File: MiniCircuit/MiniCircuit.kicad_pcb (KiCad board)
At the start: 2 copper layers, 114 x 96.5 mm, 49 parts, among them J1 Conn_02x16_Odd_Even, J2 Conn_02x05_Odd_Even, SW1 SW_DIP_x04, SW2 SW_DIP_x04, U1 LM6172, U2 OPA2277, U3 MCP3008, U4 MCP4921, U5 CD4066BE, U6 CD4066BE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

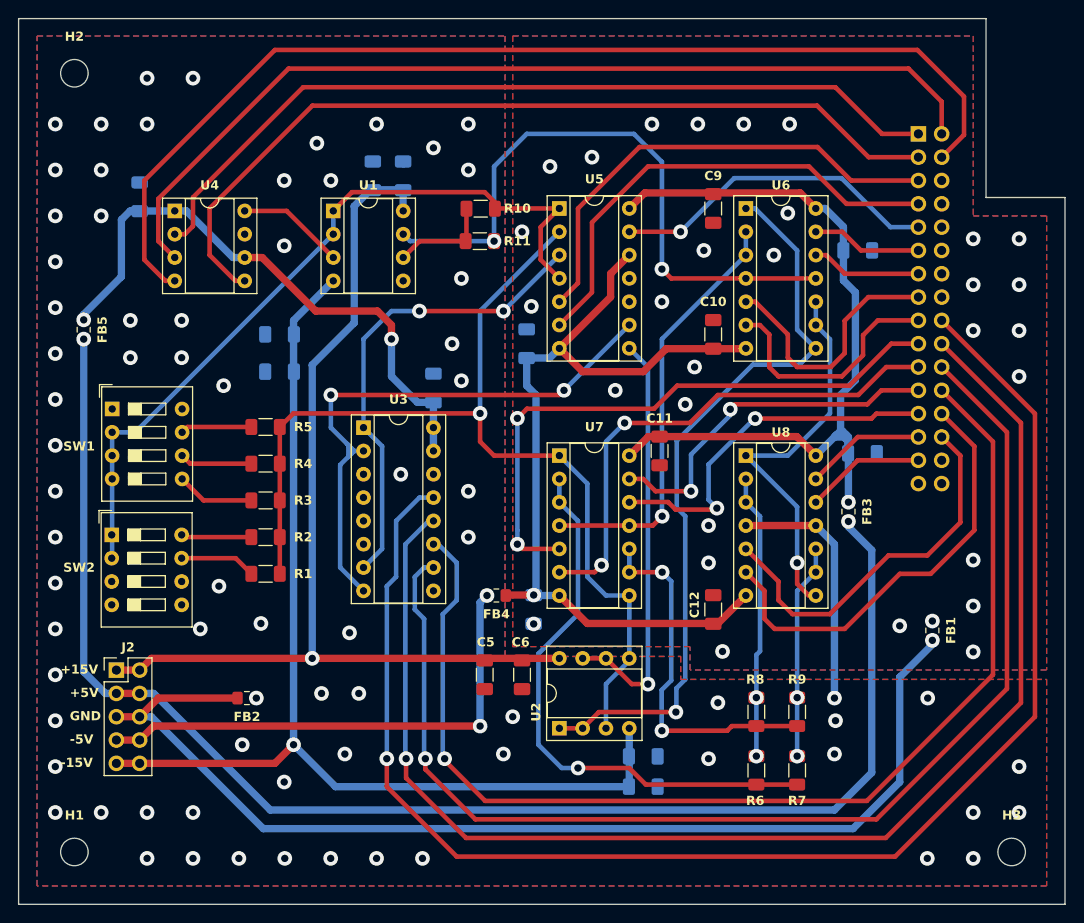
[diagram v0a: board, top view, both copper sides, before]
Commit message: Revised PCB as told by PCB Lab
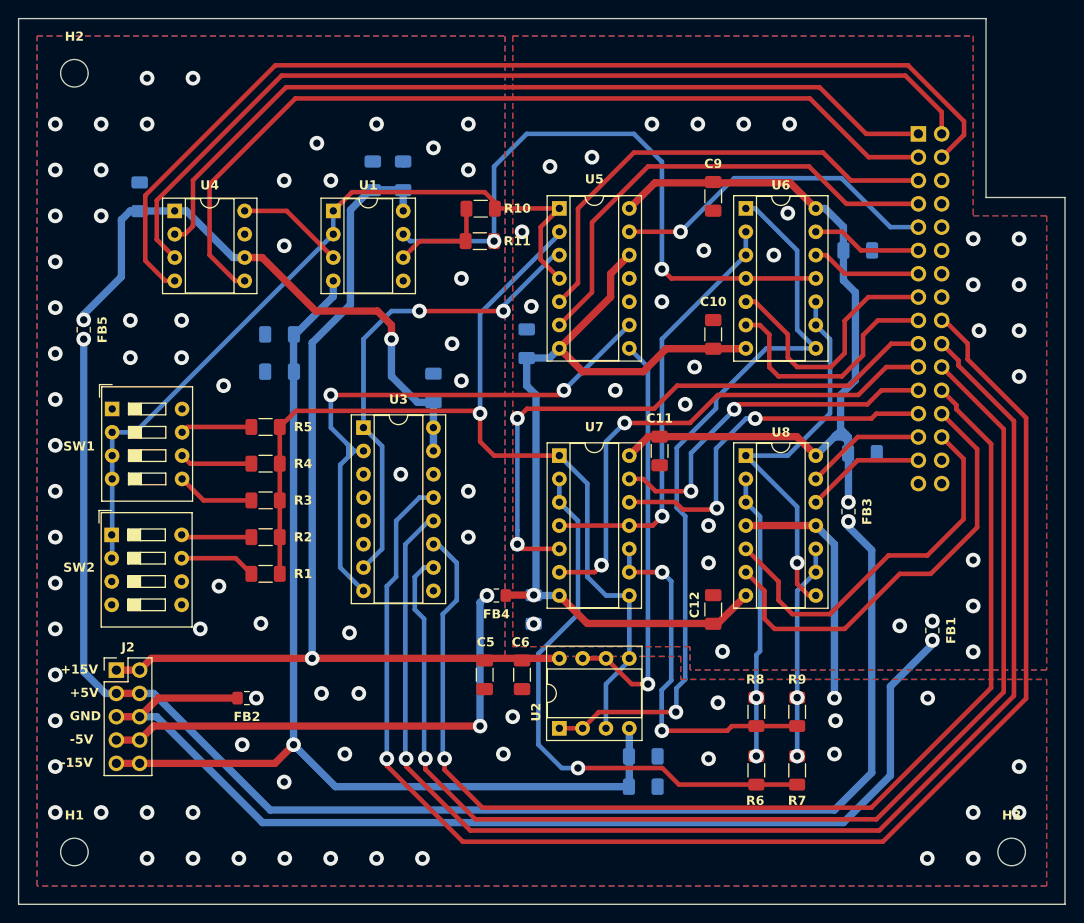
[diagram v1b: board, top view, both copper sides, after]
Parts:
- moved C9 1.32 mm to (201.7, 42.9)
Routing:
- net /CLK: track 162.0 -> 156.9 mm
- net /SDI: track 117.8 -> 113.7 mm
- net /Dout: track 148.1 -> 145.2 mm
- net /LDACbar: track 94.2 -> 96.4 mm
- net /Din: track 126.2 -> 127.9 mm
- net /PowerGND: track 120.9 -> 119.3 mm
- net /SCK: track 103.4 -> 102.2 mm
- net /DAC_CSbar: track 91.6 -> 92.7 mm
- net /+5VD: track 87.8 -> 88.7 mm
